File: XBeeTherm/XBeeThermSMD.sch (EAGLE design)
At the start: 27 parts

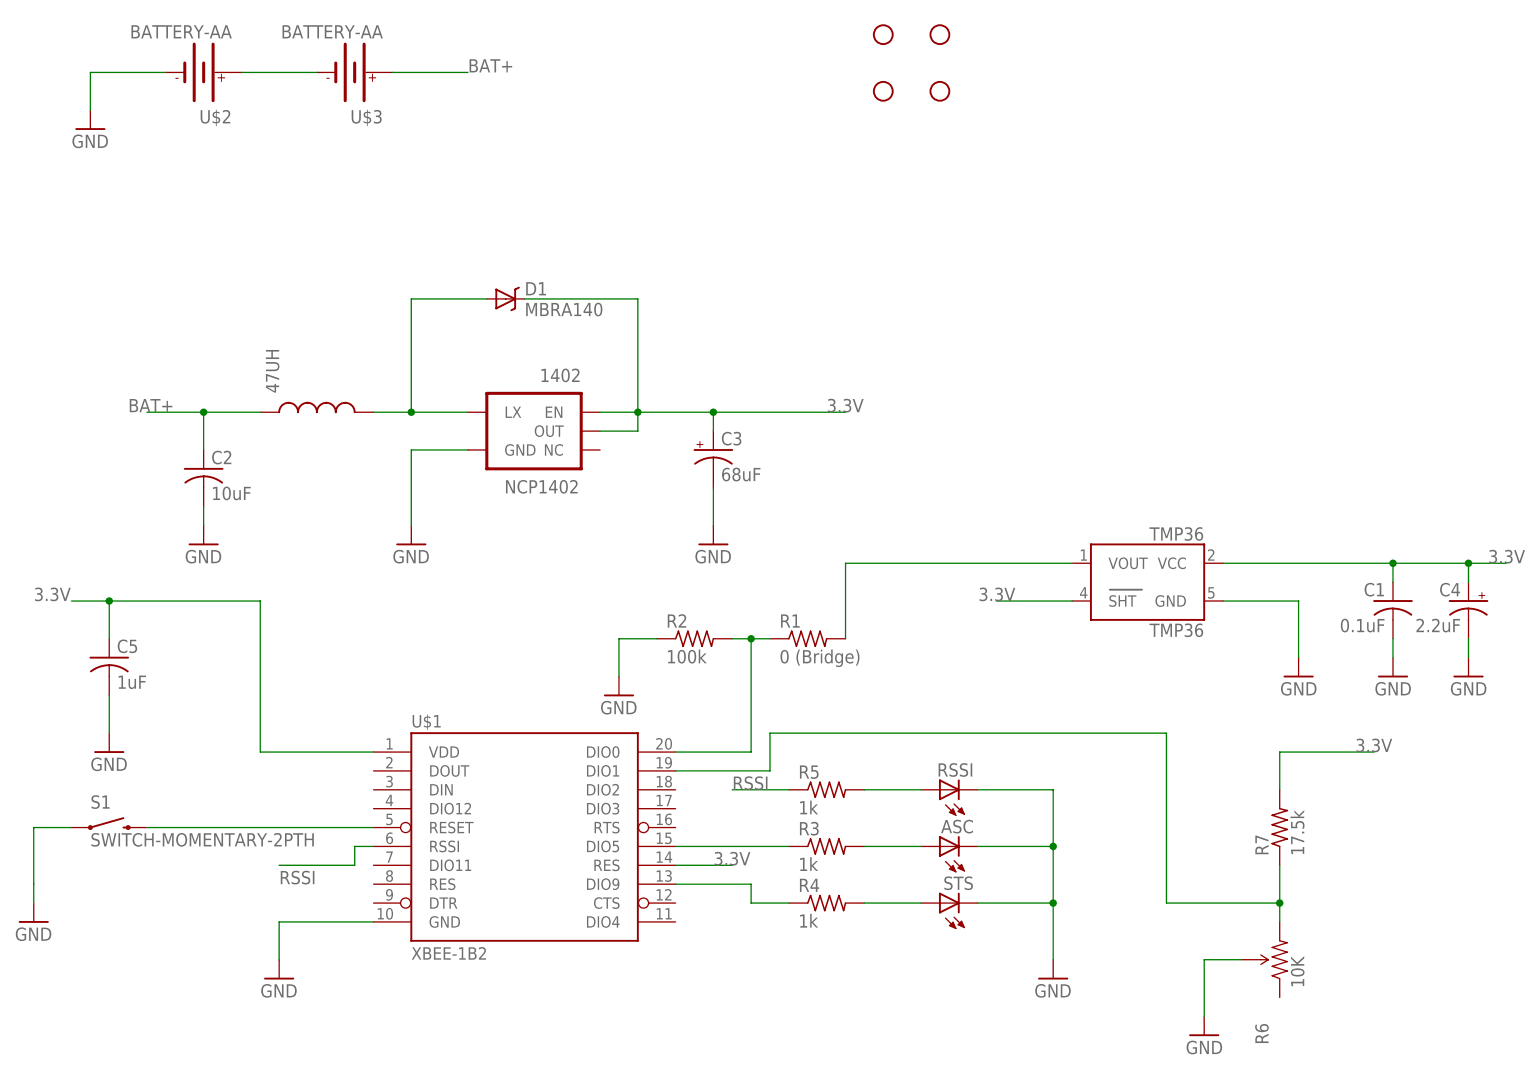
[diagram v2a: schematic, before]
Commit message: Adding battery undervoltage protection
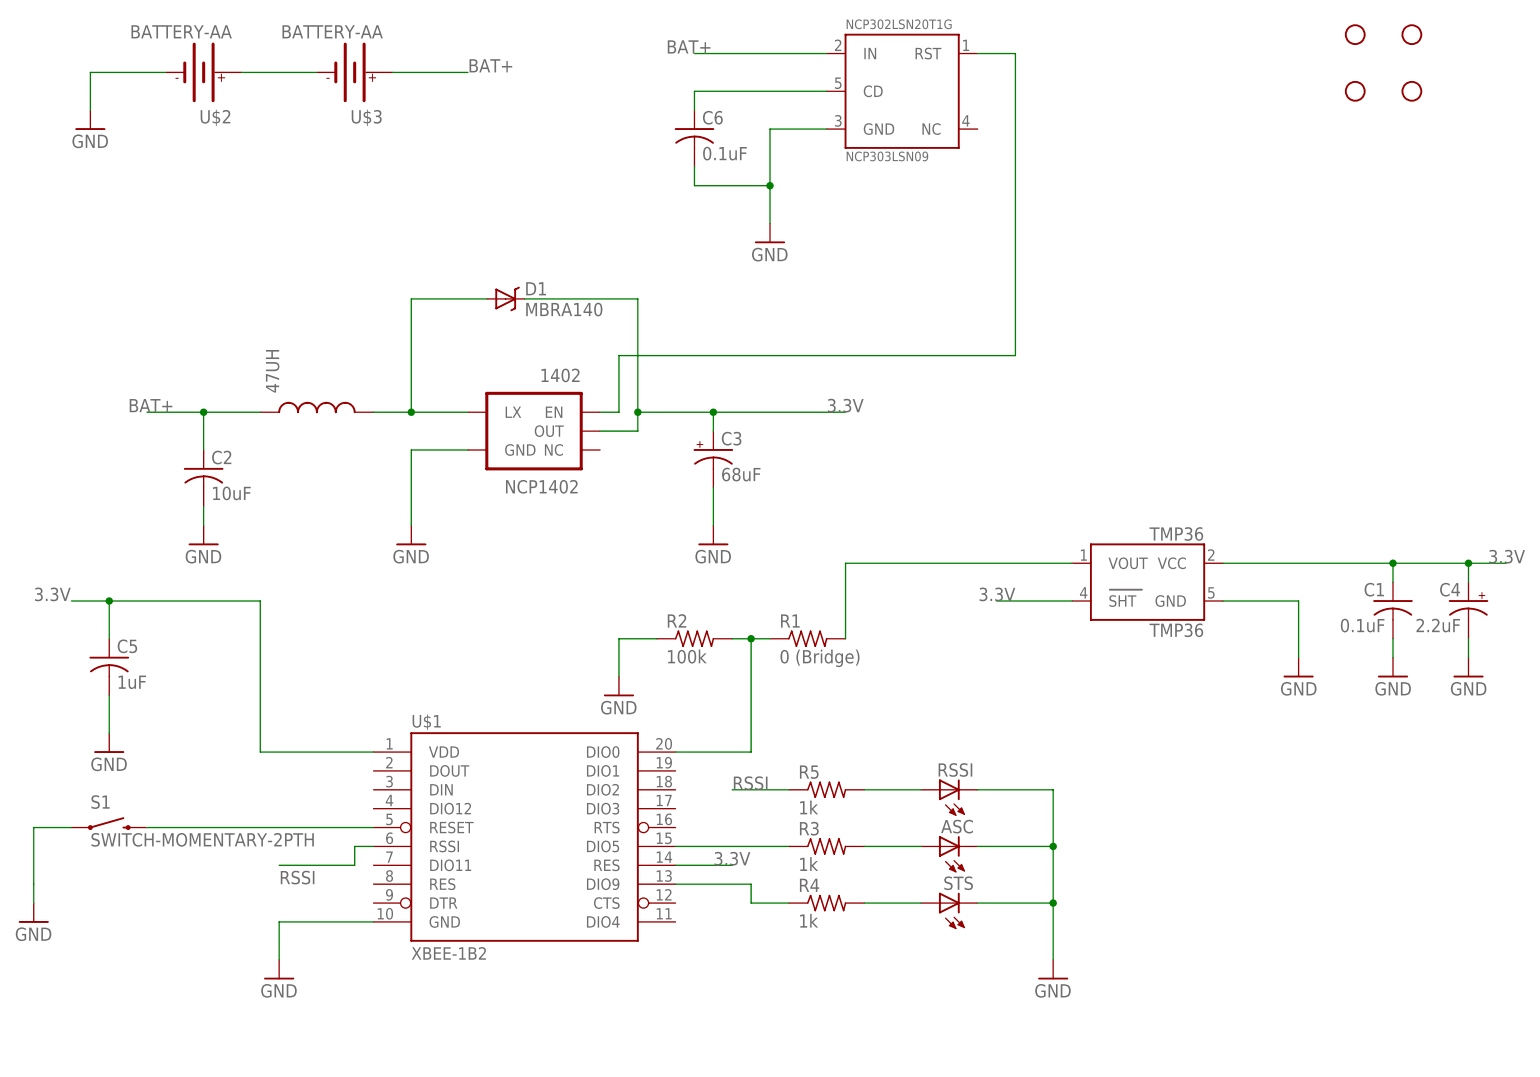
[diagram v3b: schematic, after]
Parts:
- removed R6: 10K, SparkFun-Electromechanical:TRIMPOT-2
- removed R7: 17.5k, resistor:R-US_R0603
- added C6: 0.1uF, rcl:C-USC0402
- added NCP302LSN20T1G: NCP303LSN09, SparkFun-DigitalIC:NCP303LSN09
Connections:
- removed net N$9: R6.CW, R7.1, U$1.DIO1
- new net N$11: C6.1, NCP302LSN20T1G.CD
- new net N$12: 1402.EN, NCP302LSN20T1G.RST
- net 3.3V: no longer 1402.EN, R7.2
- net BAT+: now also NCP302LSN20T1G.IN
- net GND: now also C6.2, NCP302LSN20T1G.GND; no longer R6.WIPER
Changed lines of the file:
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@@
 <setting verticaltext="up"/>
 </settings>
-<grid distance="0.1" unitdist="inch" unit="inch" style="lines" multiple="1" display="no" altdistance="0.01" altunitdist="inch" altunit="inch"/>
+<grid distance="0.05" unitdist="inch" unit="inch" style="lines" multiple="1" display="yes" altdistance="0.005" altunitdist="inch" altunit="inch"/>
 <layers>
 <layer number="1" name="Top" color="4" fill="1" visible="no" active="no"/>
@@
 <part name="RSSI" library="led" deviceset="LED" device="CHIP-LED0603"/>
 <part name="R5" library="resistor" deviceset="R-US_" device="R0603" value="1k"/>
-<part name="R6" library="SparkFun-Electromechanical" deviceset="TRIMPOT" device="-2" value="10K"/>
-<part name="GND13" library="SparkFun-Aesthetics" deviceset="GND" device=""/>
-<part name="R7" library="resistor" deviceset="R-US_" device="R0603" value="17.5k"/>
+<part name="NCP302LSN20T1G" library="SparkFun-DigitalIC" deviceset="NCP303LSN09" device=""/>
+<part name="GND14" library="SparkFun-Aesthetics" deviceset="GND" device=""/>
+<part name="C6" library="rcl" deviceset="C-US" device="C0402" value="0.1uF"/>
 </parts>
 <sheets>
@@
 <instance part="C5" gate="G$1" x="27.94" y="101.6"/>
 <instance part="GND10" gate="1" x="27.94" y="88.9"/>
-<instance part="STANDOFF1" gate="G$1" x="132.08" y="185.42"/>
-<instance part="STANDOFF2" gate="G$1" x="139.7" y="185.42"/>
-<instance part="STANDOFF3" gate="G$1" x="132.08" y="177.8"/>
-<instance part="STANDOFF4" gate="G$1" x="139.7" y="177.8"/>
+<instance part="STANDOFF1" gate="G$1" x="195.58" y="185.42"/>
+<instance part="STANDOFF2" gate="G$1" x="203.2" y="185.42"/>
+<instance part="STANDOFF3" gate="G$1" x="195.58" y="177.8"/>
+<instance part="STANDOFF4" gate="G$1" x="203.2" y="177.8"/>
 <instance part="STS" gate="G$1" x="139.7" y="68.58" rot="R90"/>
 <instance part="ASC" gate="G$1" x="139.7" y="76.2" rot="R90"/>
@@
 <instance part="RSSI" gate="G$1" x="139.7" y="83.82" rot="R90"/>
 <instance part="R5" gate="G$1" x="124.46" y="83.82"/>
-<instance part="R6" gate="R?" x="185.42" y="60.96" rot="R90"/>
-<instance part="GND13" gate="1" x="175.26" y="50.8" rot="MR0"/>
-<instance part="R7" gate="G$1" x="185.42" y="78.74" rot="R90"/>
+<instance part="NCP302LSN20T1G" gate="G$1" x="134.62" y="177.8"/>
+<instance part="GND14" gate="1" x="116.84" y="157.48"/>
+<instance part="C6" gate="G$1" x="106.68" y="172.72"/>
 </instances>
 <busses>
@@
 <wire x1="83.82" y1="149.86" x2="99.06" y2="149.86" width="0.1524" layer="91"/>
 <wire x1="99.06" y1="149.86" x2="99.06" y2="134.62" width="0.1524" layer="91"/>
-<pinref part="1402" gate="G$1" pin="EN"/>
-<wire x1="99.06" y1="134.62" x2="93.98" y2="134.62" width="0.1524" layer="91"/>
 <wire x1="99.06" y1="134.62" x2="99.06" y2="132.08" width="0.1524" layer="91"/>
 <junction x="99.06" y="134.62"/>
@@
 <wire x1="104.14" y1="73.66" x2="111.76" y2="73.66" width="0.1524" layer="91"/>
 <label x="109.22" y="73.66" size="1.778" layer="95"/>
-</segment>
-<segment>
-<pinref part="R7" gate="G$1" pin="2"/>
-<wire x1="185.42" y1="83.82" x2="185.42" y2="88.9" width="0.1524" layer="91"/>
-<wire x1="185.42" y1="88.9" x2="198.12" y2="88.9" width="0.1524" layer="91"/>
-<label x="195.58" y="88.9" size="1.778" layer="95"/>
 </segment>
 </net>
@@
 </segment>
 <segment>
-<pinref part="GND13" gate="1" pin="GND"/>
-<wire x1="175.26" y1="53.34" x2="175.26" y2="60.96" width="0.1524" layer="91"/>
-<pinref part="R6" gate="R?" pin="WIPER"/>
-<wire x1="175.26" y1="60.96" x2="180.34" y2="60.96" width="0.1524" layer="91"/>
+<pinref part="NCP302LSN20T1G" gate="G$1" pin="GND"/>
+<wire x1="124.46" y1="172.72" x2="116.84" y2="172.72" width="0.1524" layer="91"/>
+<pinref part="GND14" gate="1" pin="GND"/>
+<wire x1="116.84" y1="172.72" x2="116.84" y2="165.1" width="0.1524" layer="91"/>
+<wire x1="116.84" y1="165.1" x2="116.84" y2="160.02" width="0.1524" layer="91"/>
+<wire x1="106.68" y1="167.64" x2="106.68" y2="165.1" width="0.1524" layer="91"/>
+<wire x1="106.68" y1="165.1" x2="116.84" y2="165.1" width="0.1524" layer="91"/>
+<junction x="116.84" y="165.1"/>
+<pinref part="C6" gate="G$1" pin="2"/>
 </segment>
 </net>
@@
 <wire x1="66.04" y1="180.34" x2="76.2" y2="180.34" width="0.1524" layer="91"/>
 <label x="76.2" y="180.34" size="1.778" layer="95"/>
+</segment>
+<segment>
+<pinref part="NCP302LSN20T1G" gate="G$1" pin="IN"/>
+<wire x1="124.46" y1="182.88" x2="106.68" y2="182.88" width="0.1524" layer="91"/>
+<label x="102.87" y="182.88" size="1.778" layer="95"/>
 </segment>
 </net>
@@
 </segment>
 </net>
-<net name="N$9" class="0">
-<segment>
-<pinref part="R7" gate="G$1" pin="1"/>
-<pinref part="R6" gate="R?" pin="CW"/>
-<wire x1="185.42" y1="73.66" x2="185.42" y2="68.58" width="0.1524" layer="91"/>
-<wire x1="185.42" y1="68.58" x2="185.42" y2="66.04" width="0.1524" layer="91"/>
-<wire x1="185.42" y1="68.58" x2="170.18" y2="68.58" width="0.1524" layer="91"/>
-<junction x="185.42" y="68.58"/>
-<wire x1="170.18" y1="68.58" x2="170.18" y2="91.44" width="0.1524" layer="91"/>
-<wire x1="170.18" y1="91.44" x2="116.84" y2="91.44" width="0.1524" layer="91"/>
-<wire x1="116.84" y1="91.44" x2="116.84" y2="86.36" width="0.1524" layer="91"/>
-<pinref part="U$1" gate="G$1" pin="DIO1"/>
-<wire x1="116.84" y1="86.36" x2="104.14" y2="86.36" width="0.1524" layer="91"/>
-</segment>
-</net>
+<net name="N$11" class="0">
+<segment>
+<pinref part="NCP302LSN20T1G" gate="G$1" pin="CD"/>
+<wire x1="124.46" y1="177.8" x2="106.68" y2="177.8" width="0.1524" layer="91"/>
+<wire x1="106.68" y1="177.8" x2="106.68" y2="175.26" width="0.1524" layer="91"/>
+<pinref part="C6" gate="G$1" pin="1"/>
+</segment>
+</net>
+<net name="N$12" class="0">
+<segment>
+<pinref part="1402" gate="G$1" pin="EN"/>
+<wire x1="93.98" y1="134.62" x2="96.52" y2="134.62" width="0.1524" layer="91"/>
+<wire x1="96.52" y1="134.62" x2="96.52" y2="142.24" width="0.1524" layer="91"/>
+<wire x1="96.52" y1="142.24" x2="149.86" y2="142.24" width="0.1524" layer="91"/>
+<wire x1="149.86" y1="142.24" x2="149.86" y2="182.88" width="0.1524" layer="91"/>
+<pinref part="NCP302LSN20T1G" gate="G$1" pin="RST"/>
+<wire x1="149.86" y1="182.88" x2="144.78" y2="182.88" width="0.1524" layer="91"/>
+</segment>
+</net>
